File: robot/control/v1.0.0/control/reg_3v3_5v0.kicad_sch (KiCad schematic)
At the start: 25 parts, among them U3 LTC3636

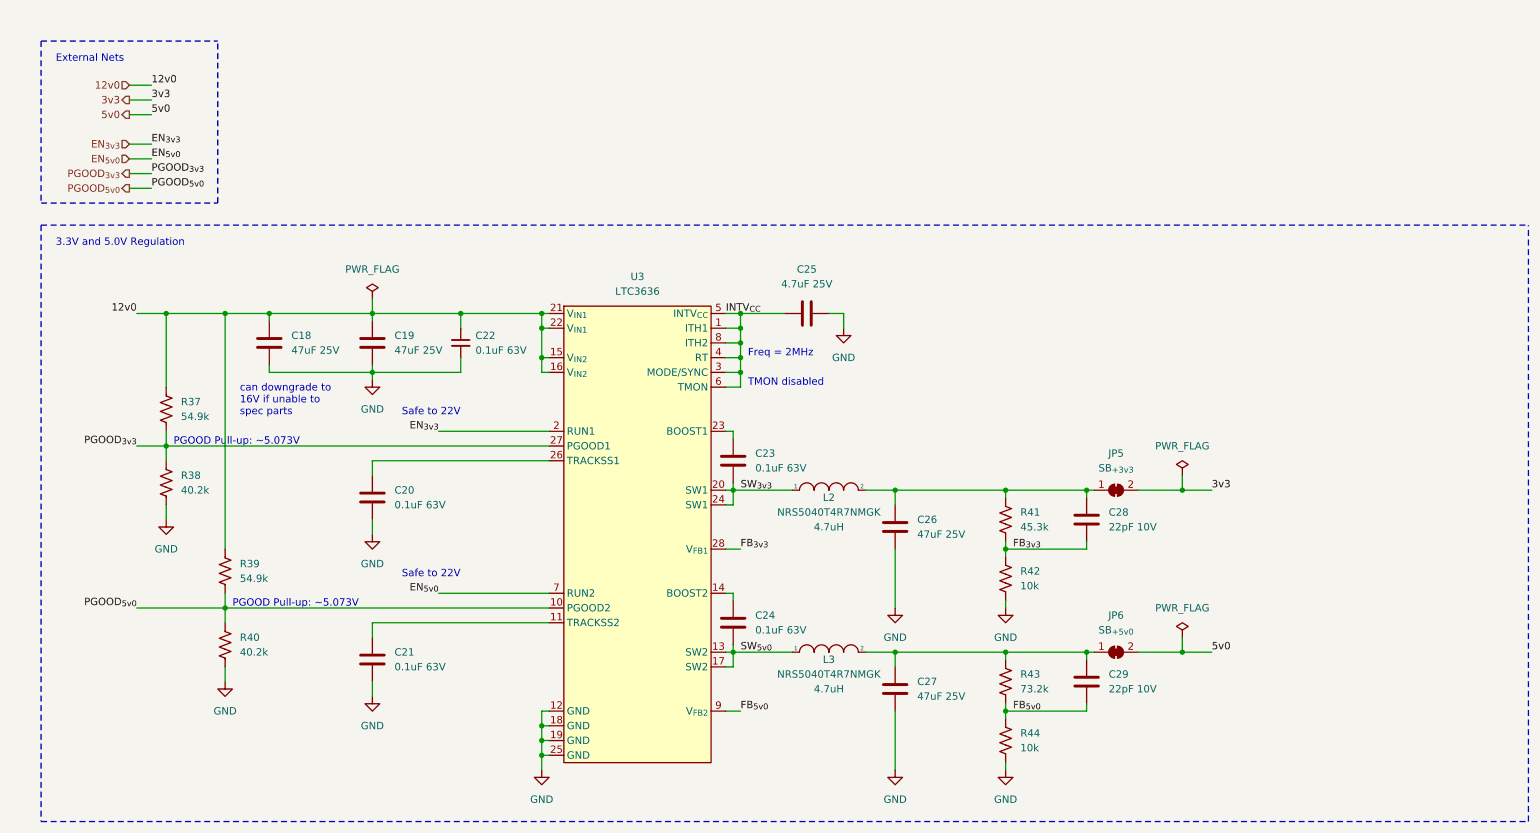
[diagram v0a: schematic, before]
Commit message: Control schematic (sans crystal oscillators)
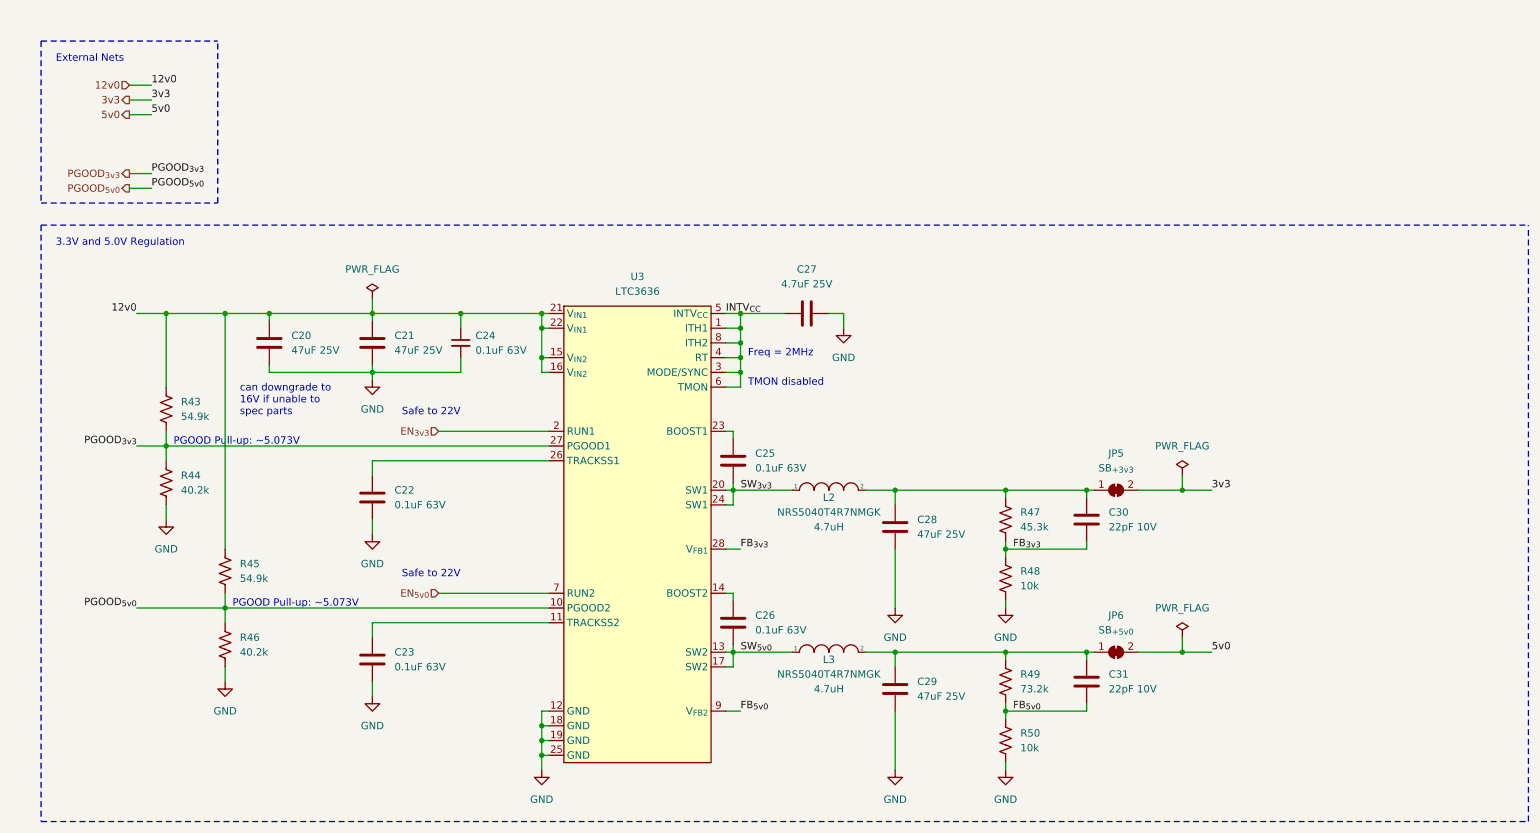
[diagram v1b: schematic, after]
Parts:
- renumbered C18 to C20, C19 to C21, C20 to C22, C21 to C23, C22 to C24, C23 to C25, C24 to C26, C25 to C27, C26 to C28, C27 to C29, C28 to C30, C29 to C31, R37 to R43, R38 to R44, R39 to R45, R40 to R46, R41 to R47, R42 to R48, R43 to R49, R44 to R50
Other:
- title: Bodge Control -> Control

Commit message: Control v1.0.0
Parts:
- renumbered C20 to C19, C21 to C20, C22 to C21, C23 to C22, C24 to C23, C25 to C24, C26 to C25, C27 to C26, C28 to C27, C29 to C28, C30 to C29, C31 to C30, R43 to R45, R44 to R46, R45 to R47, R46 to R48, R47 to R49, R48 to R50, R49 to R51, R50 to R52
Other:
- note removed: "External Nets"
- moved on the sheet: C19, C20, C21, C22, C23, C24, C25, C26, C27, C28, C29, C30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
